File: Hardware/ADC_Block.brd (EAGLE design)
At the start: 30.5 x 44.5 mm, 31 parts, among them U1 ADS1015, U2 PCA9306, U3 3.3V

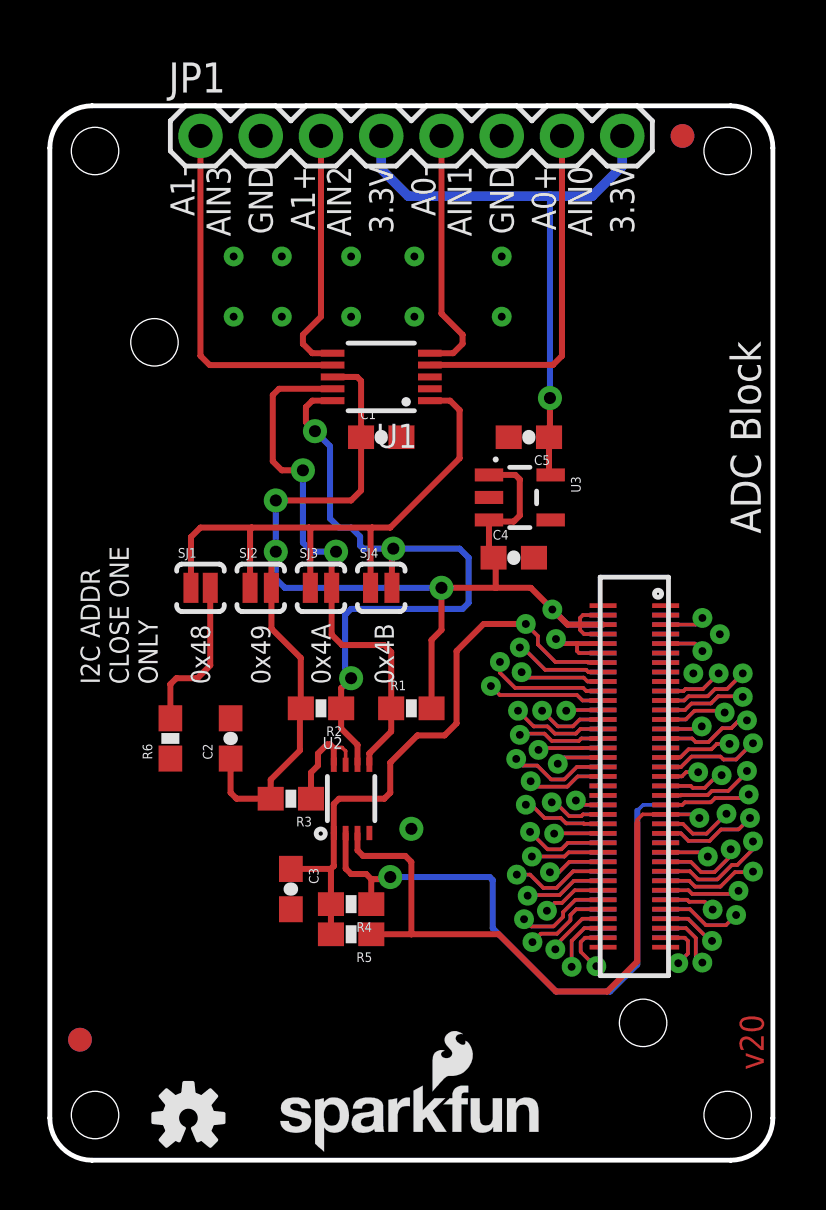
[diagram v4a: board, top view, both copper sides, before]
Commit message: changing pour layers
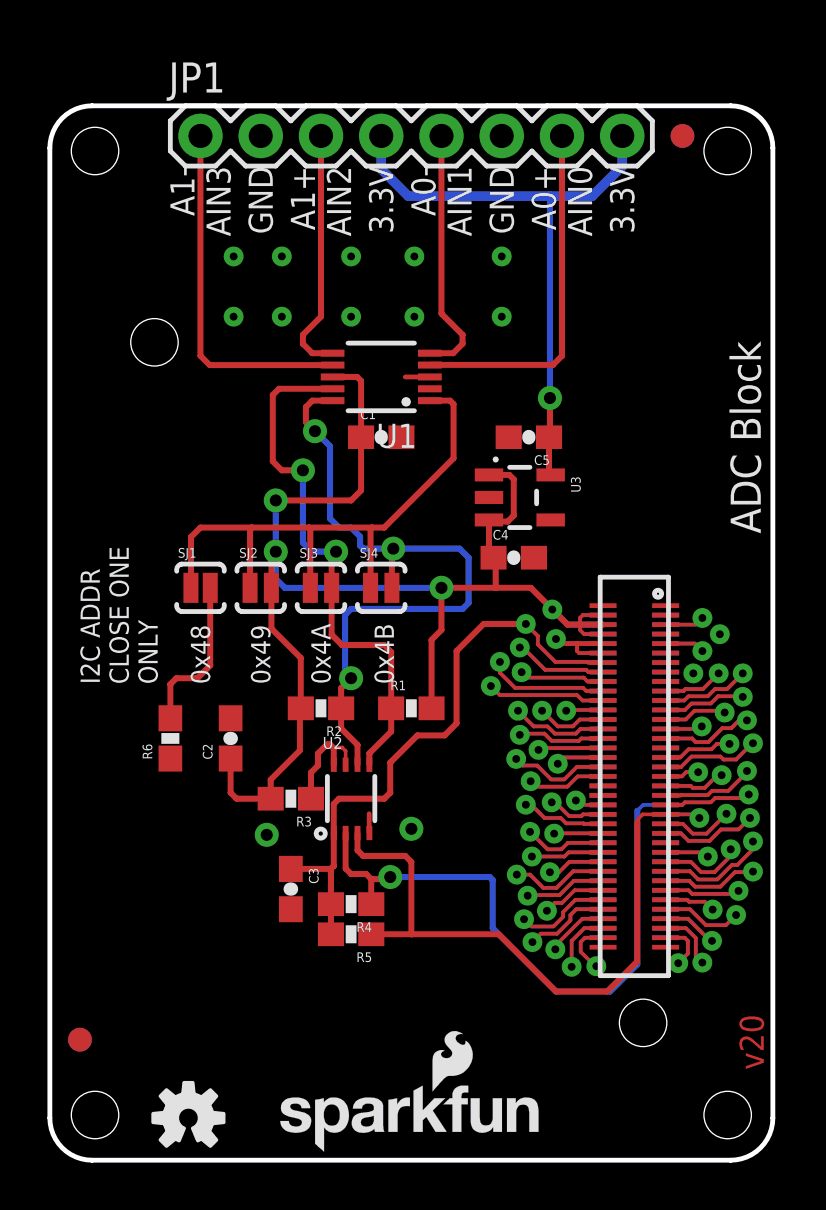
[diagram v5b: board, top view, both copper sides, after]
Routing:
- net GND: track 0.00 -> 1.85 mm, vias 13 -> 14
- net VSYS: track 64.6 -> 64.1 mm
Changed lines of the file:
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@@
 <signals>
 <signal name="GND">
-<polygon width="0.1524" layer="16" spacing="0.254" isolate="0.03048125" rank="6">
+<polygon width="0.1524" layer="16" spacing="0.254" isolate="0.2032" rank="6">
 <vertex x="30.48" y="42.672"/>
 <vertex x="30.48" y="1.778" curve="-90"/>
@@
 <vertex x="28.702" y="44.45" curve="-90"/>
 </polygon>
-<polygon width="0.1524" layer="1" spacing="0.254" isolate="0.03048125" rank="6">
+<polygon width="0.1524" layer="1" spacing="0.254" isolate="0.2032" rank="6">
 <vertex x="30.48" y="1.728" curve="-90"/>
 <vertex x="28.752" y="0"/>
@@
 <via x="7.747" y="38.1" extent="1-16" drill="0.3302"/>
 <via x="7.747" y="35.56" extent="1-16" drill="0.3302"/>
+<wire x1="13.47" y1="13.7938" x2="13.462" y2="13.7938" width="0.2032" layer="1"/>
+<wire x1="13.462" y1="13.7938" x2="13.462" y2="14.605" width="0.2032" layer="1"/>
+<via x="9.144" y="13.716" extent="1-16" drill="0.508"/>
+<wire x1="16.02" y1="33.02" x2="14.986" y2="33.02" width="0.2032" layer="1"/>
+<wire x1="25.96" y1="22.9798" x2="25.96" y2="22.98" width="0" layer="19" extent="1-16"/>
+<wire x1="25.96" y1="22.18" x2="25.96" y2="22.98" width="0" layer="19" extent="16-16"/>
+<wire x1="25.96" y1="22.1798" x2="25.96" y2="22.18" width="0" layer="19" extent="1-16"/>
+<wire x1="25.96" y1="21.38" x2="25.96" y2="22.18" width="0" layer="19" extent="16-16"/>
+<wire x1="25.96" y1="21.3798" x2="25.96" y2="21.38" width="0" layer="19" extent="1-16"/>
+<wire x1="25.96" y1="20.98" x2="25.96" y2="21.38" width="0" layer="19" extent="16-16"/>
+<wire x1="25.96" y1="20.9798" x2="25.96" y2="20.98" width="0" layer="19" extent="1-16"/>
+<wire x1="25.96" y1="20.58" x2="25.96" y2="20.98" width="0" layer="19" extent="16-16"/>
+<wire x1="25.96" y1="20.5798" x2="25.96" y2="20.58" width="0" layer="19" extent="1-16"/>
+<wire x1="25.96" y1="20.18" x2="25.96" y2="20.58" width="0" layer="19" extent="16-16"/>
+<wire x1="25.96" y1="20.1798" x2="25.96" y2="20.18" width="0" layer="19" extent="1-16"/>
+<wire x1="27.1272" y1="20.5232" x2="25.96" y2="20.58" width="0" layer="19" extent="16-16"/>
+<wire x1="28.2448" y1="22.1742" x2="27.1272" y2="20.5232" width="0" layer="19" extent="1-1"/>
 </signal>
 <signal name="VSYS">
@@
 <wire x1="18.5119" y1="26.924" x2="18.5119" y2="25.5961" width="0.254" layer="1"/>
 <wire x1="18.5119" y1="25.5961" x2="18.708" y2="25.4" width="0.254" layer="1"/>
-<wire x1="18.5119" y1="28.89" x2="19.624" y2="28.89" width="0.254" layer="1"/>
-<wire x1="19.624" y1="28.89" x2="19.812" y2="28.702" width="0.254" layer="1"/>
-<wire x1="19.812" y1="28.702" x2="19.812" y2="27.178" width="0.254" layer="1"/>
-<wire x1="19.812" y1="27.178" x2="19.558" y2="26.924" width="0.254" layer="1"/>
-<wire x1="19.558" y1="26.924" x2="18.5119" y2="26.924" width="0.254" layer="1"/>
+<wire x1="18.5119" y1="28.89" x2="19.37" y2="28.89" width="0.254" layer="1"/>
+<wire x1="19.37" y1="28.89" x2="19.558" y2="28.702" width="0.254" layer="1"/>
+<wire x1="19.558" y1="28.702" x2="19.558" y2="27.178" width="0.254" layer="1"/>
+<wire x1="19.558" y1="27.178" x2="19.304" y2="26.924" width="0.254" layer="1"/>
+<wire x1="19.304" y1="26.924" x2="18.5119" y2="26.924" width="0.254" layer="1"/>
 </signal>
 <signal name="3.3V">
@@
 <wire x1="8.509" y1="26.67" x2="10.922" y2="26.67" width="0.254" layer="1"/>
 <wire x1="10.922" y1="26.67" x2="13.589" y2="26.67" width="0.254" layer="1"/>
-<wire x1="13.589" y1="26.67" x2="14.351" y2="26.67" width="0.254" layer="1"/>
-<wire x1="14.351" y1="26.67" x2="17.272" y2="29.591" width="0.254" layer="1"/>
-<wire x1="17.272" y1="29.591" x2="17.272" y2="31.623" width="0.254" layer="1"/>
+<wire x1="13.589" y1="26.67" x2="14.097" y2="26.67" width="0.254" layer="1"/>
+<wire x1="14.097" y1="26.67" x2="17.018" y2="29.591" width="0.254" layer="1"/>
+<wire x1="17.018" y1="29.591" x2="17.018" y2="31.877" width="0.254" layer="1"/>
 <wire x1="16.02" y1="32.02" x2="16.875" y2="32.02" width="0.254" layer="1"/>
-<wire x1="16.875" y1="32.02" x2="17.272" y2="31.623" width="0.254" layer="1"/>
+<wire x1="16.875" y1="32.02" x2="17.018" y2="31.877" width="0.254" layer="1"/>
 <wire x1="8.44" y1="24.13" x2="8.44" y2="26.601" width="0.254" layer="1"/>
 <wire x1="8.44" y1="26.601" x2="8.509" y2="26.67" width="0.254" layer="1"/>

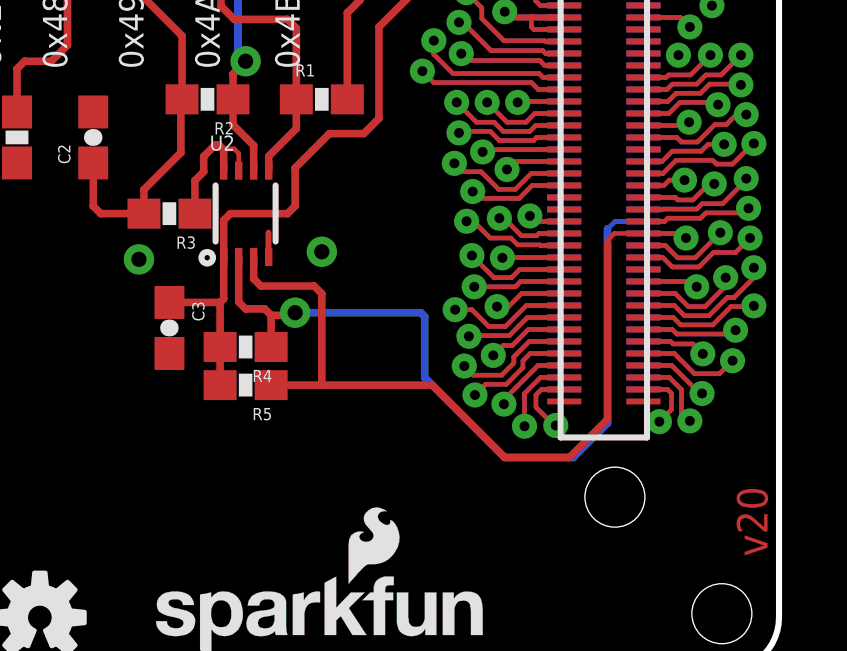
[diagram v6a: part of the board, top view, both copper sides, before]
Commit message: added Bus selection to board
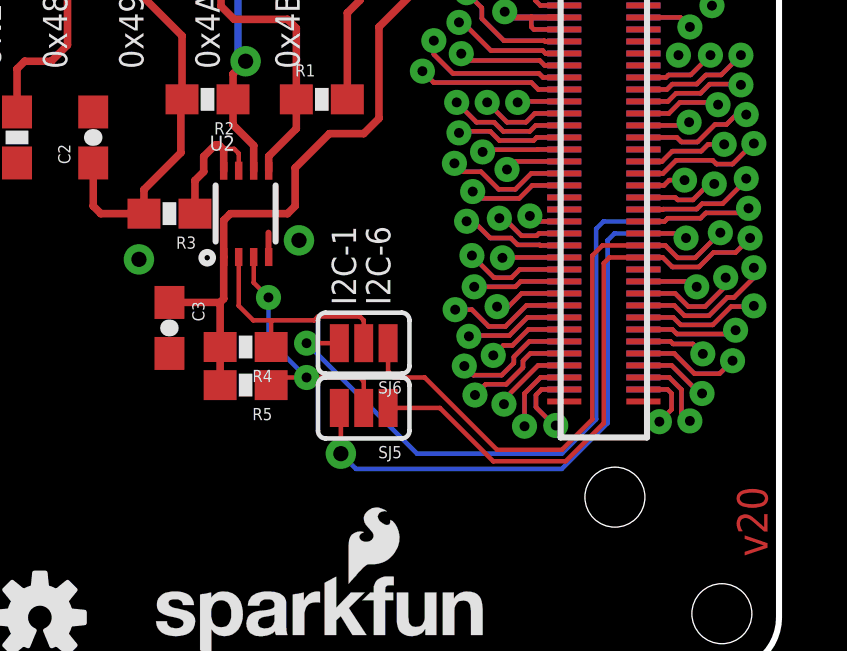
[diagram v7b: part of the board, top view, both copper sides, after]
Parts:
- added SJ5: SDA_SEL, SparkFun-Passives:PAD-JUMPER-3-2OF3_NC_BY_PASTE_YES_SILK_FULL_BOX
- added SJ6: SCL_SEL, SparkFun-Passives:PAD-JUMPER-3-2OF3_NC_BY_PASTE_YES_SILK_FULL_BOX
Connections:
- new net N$2: R4.1, SJ6.2, U2.2
- new net N$4: R5.1, SJ5.2, U2.3
- net GP19_I2C_1_SCL: now also SJ6.3; no longer R4.1, U2.2
- net GP20_I2C_1_SDA: now also SJ5.3; no longer R5.1, U2.3
- net GP27_I2C_6_SCL: now also SJ6.1
- net GP28_I2C_6_SDA: now also SJ5.1
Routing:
- net GP27_I2C_6_SCL: track 6.17 -> 22.7 mm
- net GP28_I2C_6_SDA: track 8.17 -> 23.4 mm
- net N$4: track 0.00 -> 8.88 mm, vias 0 -> 2
- net N$2: track 0.00 -> 7.75 mm
- net GP20_I2C_1_SDA: track 29.2 -> 21.6 mm, vias 1 -> 2
- net GP19_I2C_1_SCL: track 33.9 -> 28.1 mm
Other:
- board text added: "I2C-1"
- board text added: "I2C-6"
